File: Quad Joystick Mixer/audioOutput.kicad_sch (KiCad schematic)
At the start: 26 parts, among them J2 NMJ6HCD, U4 OPA1692xD

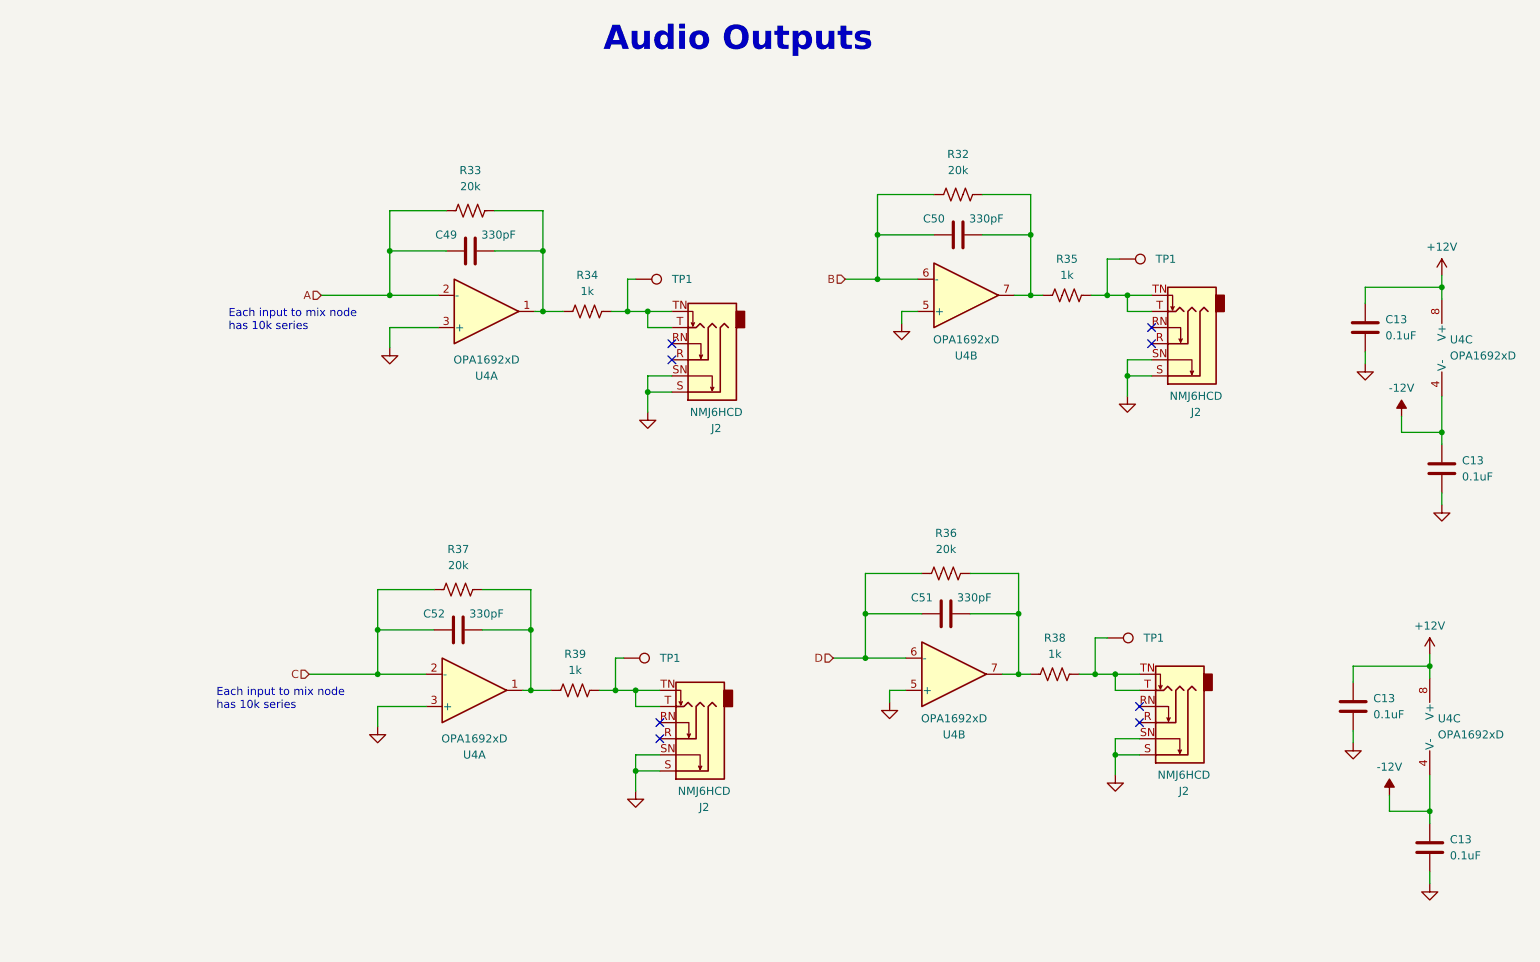
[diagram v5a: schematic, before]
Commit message: finish adding parts to the BOM
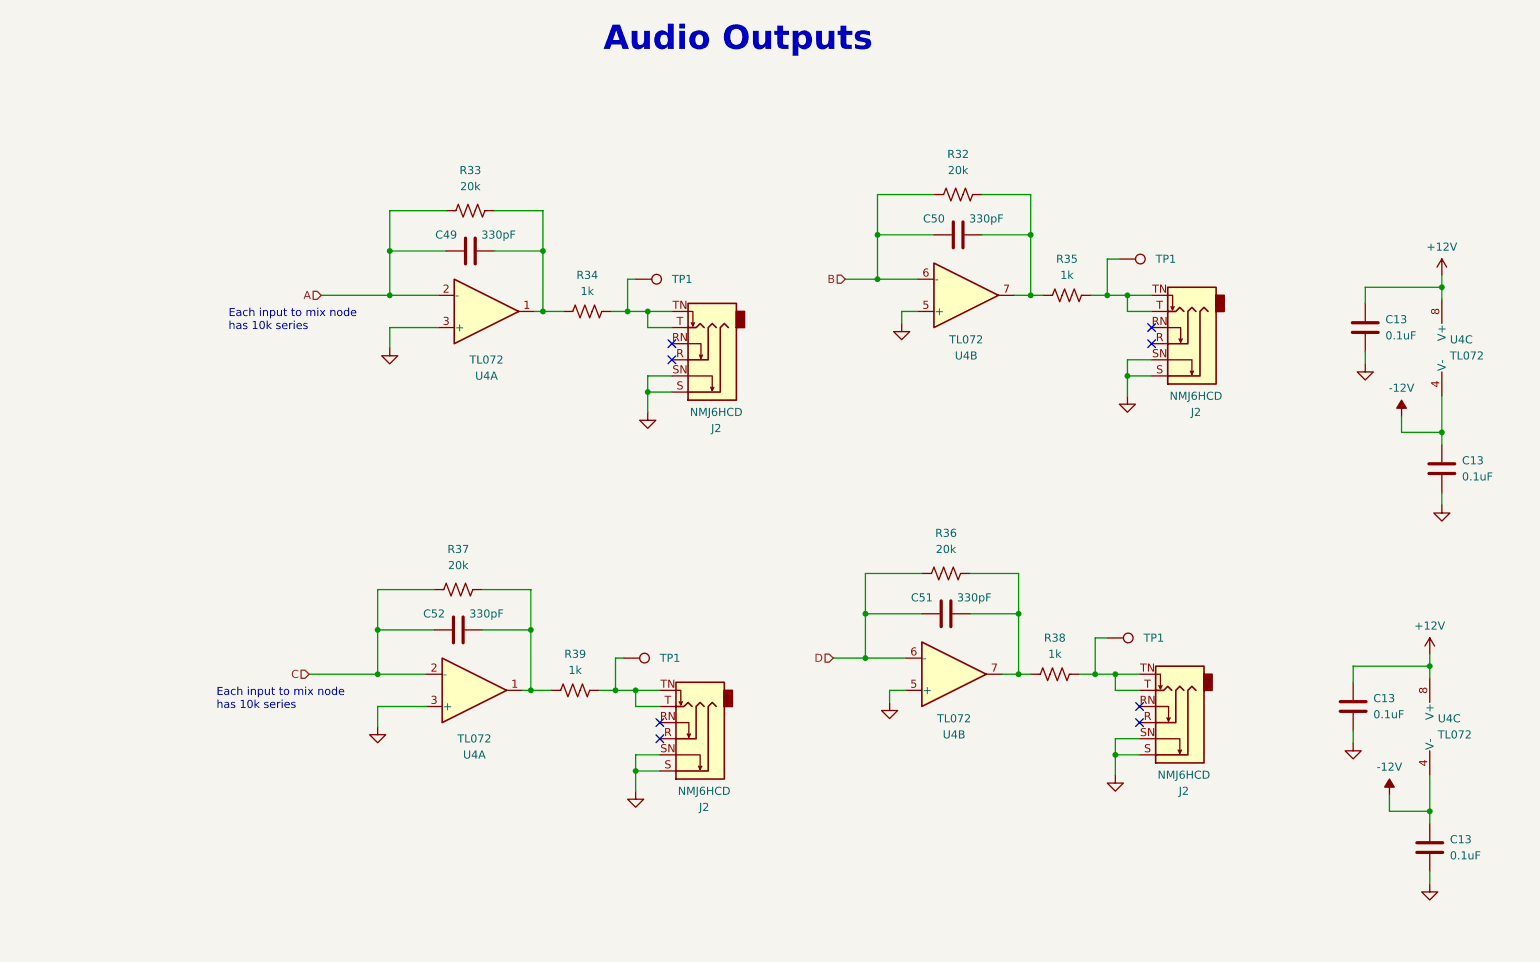
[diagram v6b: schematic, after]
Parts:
- C13, C49, C50, C51, C52: Source (none) -> DK
- J2: Source (none) -> SBP
- R32, R33, R36, R37: footprint (none) -> Resistor_SMD:R_0805_2012Metric_Pad1.20x1.40mm_HandSolder; DK PN (none) -> RMCF0805FT20K0CT-ND; MPN (none) -> RMCF0805FT20K0; Source (none) -> DK
- R34, R35, R38, R39: footprint (none) -> Resistor_SMD:R_0805_2012Metric_Pad1.20x1.40mm_HandSolder; DK PN (none) -> RMCF0805FT1K00CT-ND; MPN (none) -> RMCF0805FT1K00; Source (none) -> DK
- TP1: Source (none) -> NA
- U4: value OPA1692xD -> TL072; DK PN (none) -> 296-TL072HIDRCT-ND; MPN (none) -> TL072HIDR; Source (none) -> DK

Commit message: major layout progress
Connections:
- net at R38.1, TP1.1: now also J2.T, J2.TN; no longer J2.T, J2.TN
- net at R39.1, TP1.1: now also J2.T, J2.TN; no longer J2.T, J2.TN
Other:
- moved on the sheet: J2
